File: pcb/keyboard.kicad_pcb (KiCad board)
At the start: 2 copper layers, 225.5 x 73.5 mm, 323 parts, among them IC1 ATMEGA32U2, IC1:1 WS2811, IC1:10 WS2811, IC1:11 WS2811, IC1:12 WS2811, IC1:2 WS2811, IC1:3 WS2811, IC1:4 WS2811, IC1:5 WS2811, IC1:7 WS2811, IC1:9 WS2811, IC2:1 WS2811, IC2:10 WS2811, IC2:11 WS2811, IC2:12 WS2811, IC2:2 WS2811, IC2:3 WS2811, IC2:4 WS2811, IC2:5 WS2811, IC2:6 WS2811, IC2:7 WS2811, IC2:8 WS2811, IC2:9 WS2811, IC3:1 WS2811, IC3:10 WS2811, IC3:11 WS2811, IC3:12 WS2811, IC3:2 WS2811, IC3:3 WS2811, IC3:4 WS2811, IC3:5 WS2811, IC3:6 WS2811, IC3:7 WS2811, IC3:8 WS2811, IC3:9 WS2811, IC4:1 WS2811, IC4:10 WS2811, IC4:11 WS2811, IC4:12 WS2811, IC4:2 WS2811, IC4:3 WS2811, IC4:4 WS2811, IC4:5 WS2811, IC4:6 WS2811, IC4:7 WS2811, IC4:8 WS2811, IC4:9 WS2811, J1 USBMINI_B05, X1 7M-16.000MAAJ-T

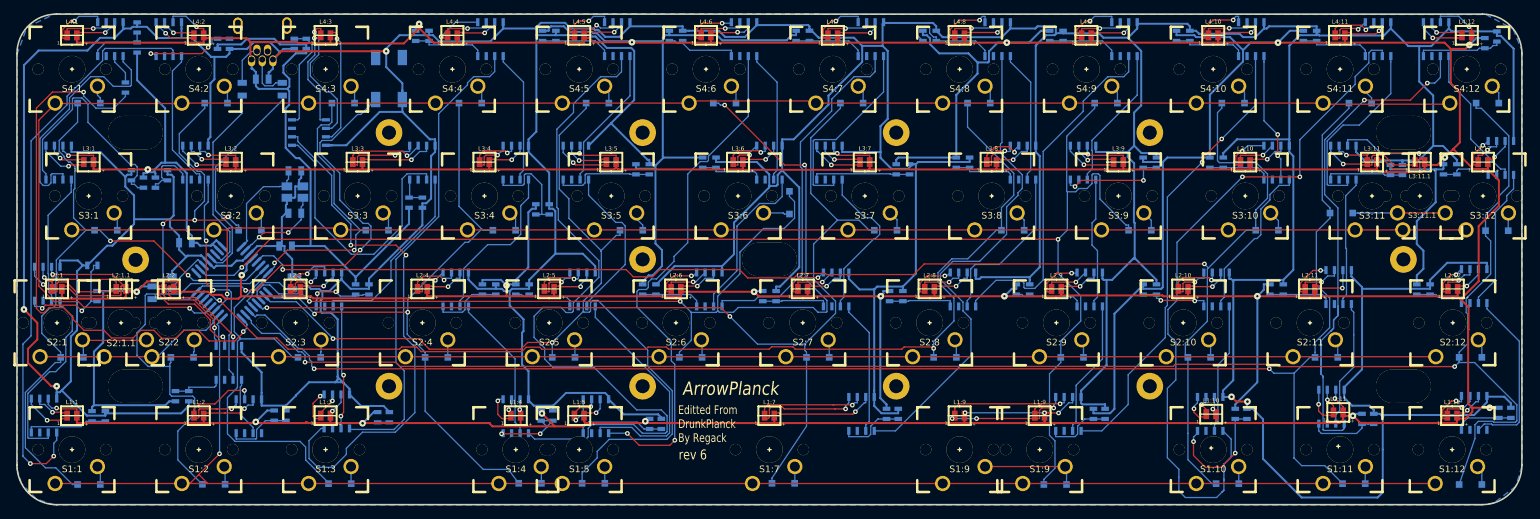
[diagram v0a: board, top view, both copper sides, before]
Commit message: add arrow keys layout
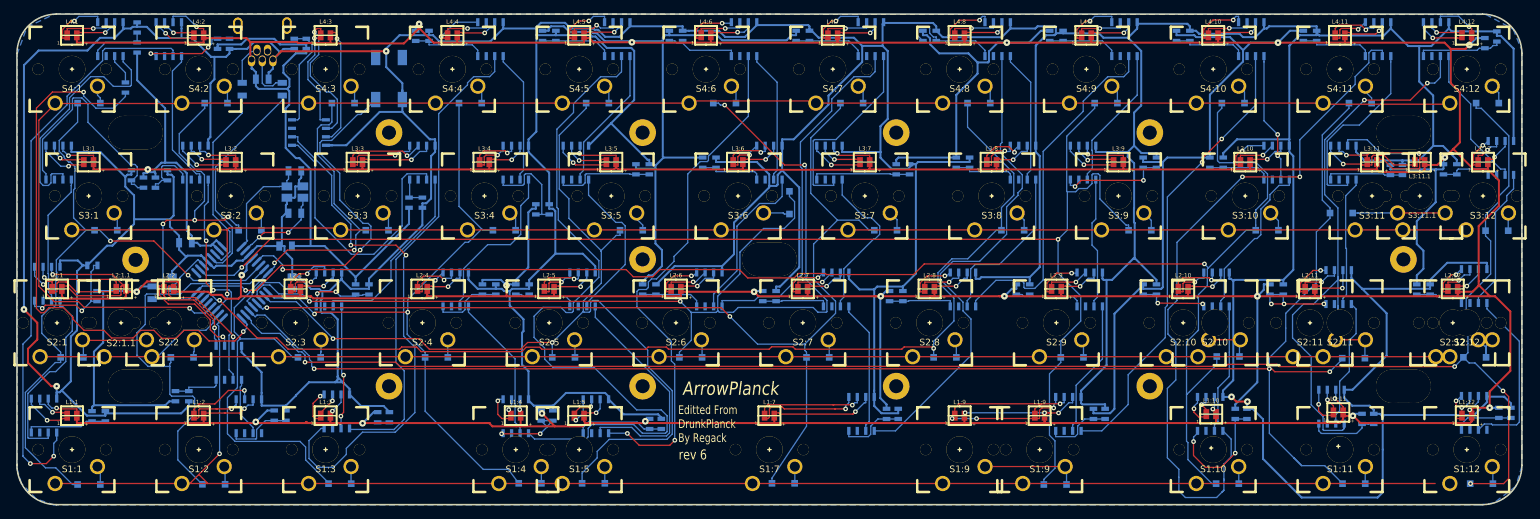
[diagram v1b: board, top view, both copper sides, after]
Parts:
- added S2:10: MX1A, CHERRY_PCB_100H_PlatedTH, F.Cu at (247.7, 131.3)
- added S2:11: MX1A, CHERRY_PCB_100H_PlatedTH, F.Cu at (266.4, 131.3)
- added S2:12: MX1A, CHERRY_PCB_125H_PlatedTH, F.Cu at (285.4, 131.3)
- moved D2:10 4.32 mm to (249.7, 136.4)
- moved D2:11 4.07 mm to (268.5, 136.7)
- moved L1:12 2.20 mm to (285.4, 150.3)
- moved S1:12 2.20 mm to (285.4, 150.3)
- moved D1:12 1.66 mm to (287.7, 155.4)
- moved D2:12 0.64 mm to (286.6, 136.5)
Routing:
- net N-00000170: track 4.78 -> 36.7 mm, vias 1 -> 2
- net VCC: track 1475.8 -> 1456.1 mm, vias 20 -> 19
- net /Matrix/col11: track 229.9 -> 240.6 mm, vias 2 -> 3
- net N-00000165: track 84.2 -> 91.6 mm
- net /Matrix/col10: track 219.0 -> 226.2 mm
- net N-0000040: track 2.76 -> 7.31 mm
- net N-0000039: track 2.78 -> 7.30 mm
- net GND: track 1310.1 -> 1314.3 mm
- net N-0000062: track 2.86 -> 6.90 mm
- net N-00000214: track 9.50 -> 13.2 mm, vias 0 -> 3
- net /Matrix/col12: track 261.4 -> 259.3 mm, vias 2 -> 4
- net N-00000171: track 5.30 -> 3.28 mm
- net N-00000172: track 6.30 -> 4.55 mm
- net N-00000106: track 10.7 -> 10.2 mm
